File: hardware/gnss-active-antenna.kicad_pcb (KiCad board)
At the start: 2 copper layers, 98 x 98 mm, 18 parts, among them J1 CONMCX002-SMD, U1 MAX2659ELT+T, U2 MIC5205-2.5YM5

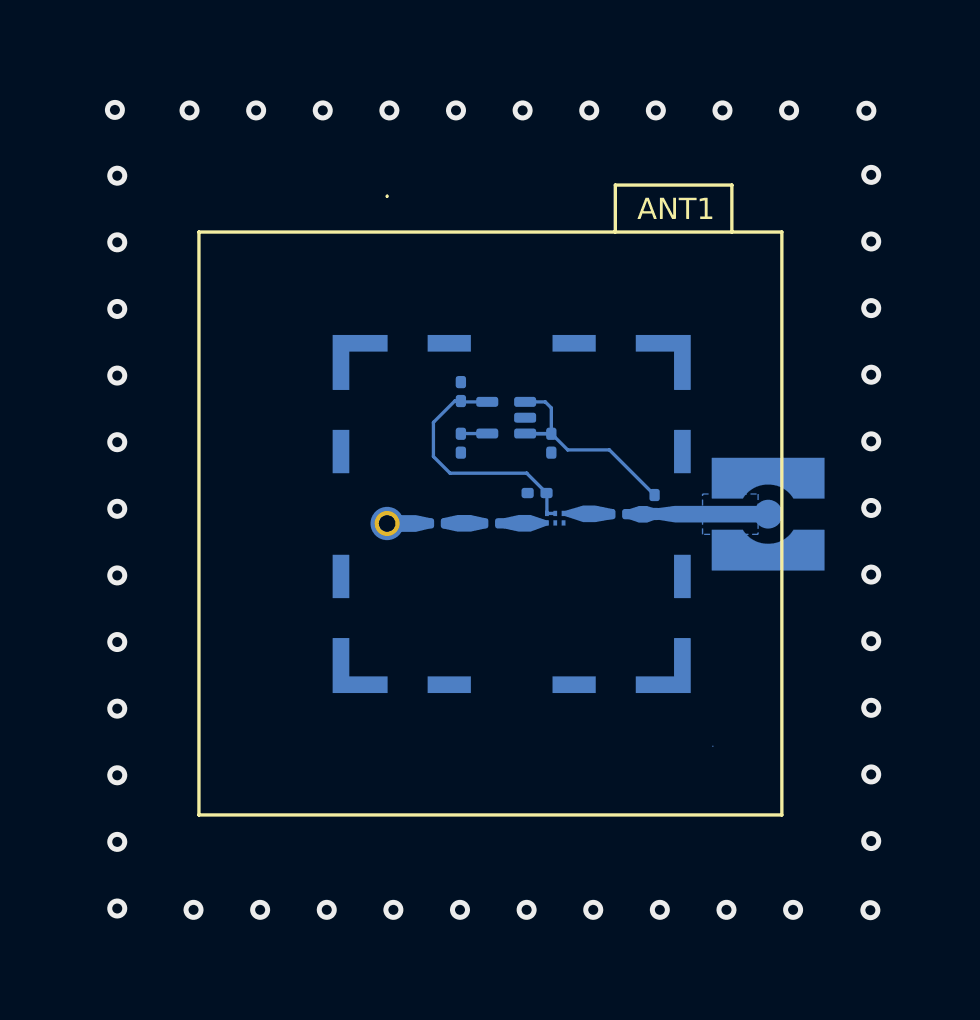
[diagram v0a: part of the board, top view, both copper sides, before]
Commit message: main: hardware: The bias-tee design was removed to make the first design simpler
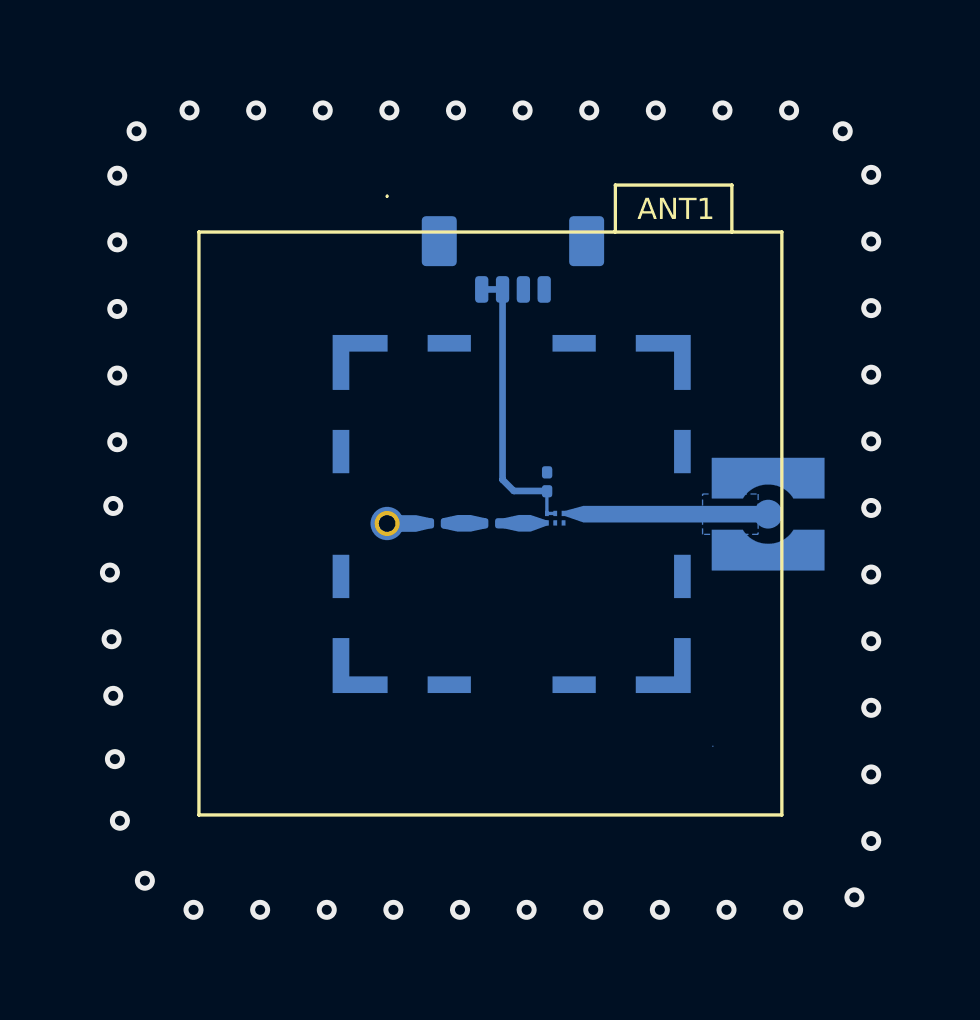
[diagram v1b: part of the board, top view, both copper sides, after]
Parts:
- removed C2: 100 pF, Capacitor_SMD:C_0402_1005Metric_Pad0.74x0.62mm_HandSolder
- removed C3: 10 uF, Capacitor_SMD:C_0402_1005Metric_Pad0.74x0.62mm_HandSolder
- removed C4: 470 pF, Capacitor_SMD:C_0402_1005Metric_Pad0.74x0.62mm_HandSolder
- removed C5: 2.2 uF, Capacitor_SMD:C_0402_1005Metric_Pad0.74x0.62mm_HandSolder
- removed L2: 82nH, Capacitor_SMD:C_0402_1005Metric_Pad0.74x0.62mm_HandSolder
- removed U2: MIC5205-2.5YM5, Package_TO_SOT_SMD:SOT-23-5
- added J2: Conn_01x04_Pin, Connector_Molex:Molex_PicoBlade_53261-0471_1x04-1MP_P1.25mm_Horizontal, B.Cu at (86.3, 64.6)
- C1: value 470pF -> 24pF
- C6: value 33 pF -> 33 nF
- H5: footprint RF_Shielding:Wuerth_36103205_20x20mm -> spacelab_lib:Wuerth_36103205_20x20mm
- L1: value 6.8 nH -> 6.2 nH
- moved C6 7.49 mm to (88.3, 78.6)
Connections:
- J1 pad 1: Net-(C2-Pad2) -> rfout
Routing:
- net 5V: track 14.2 -> 0.00 mm
- net 3V3: track 15.3 -> 17.5 mm
- net Net-(U2-BP): track 1.59 -> 0.00 mm
